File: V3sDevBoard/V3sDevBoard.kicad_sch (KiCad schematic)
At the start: 0 parts

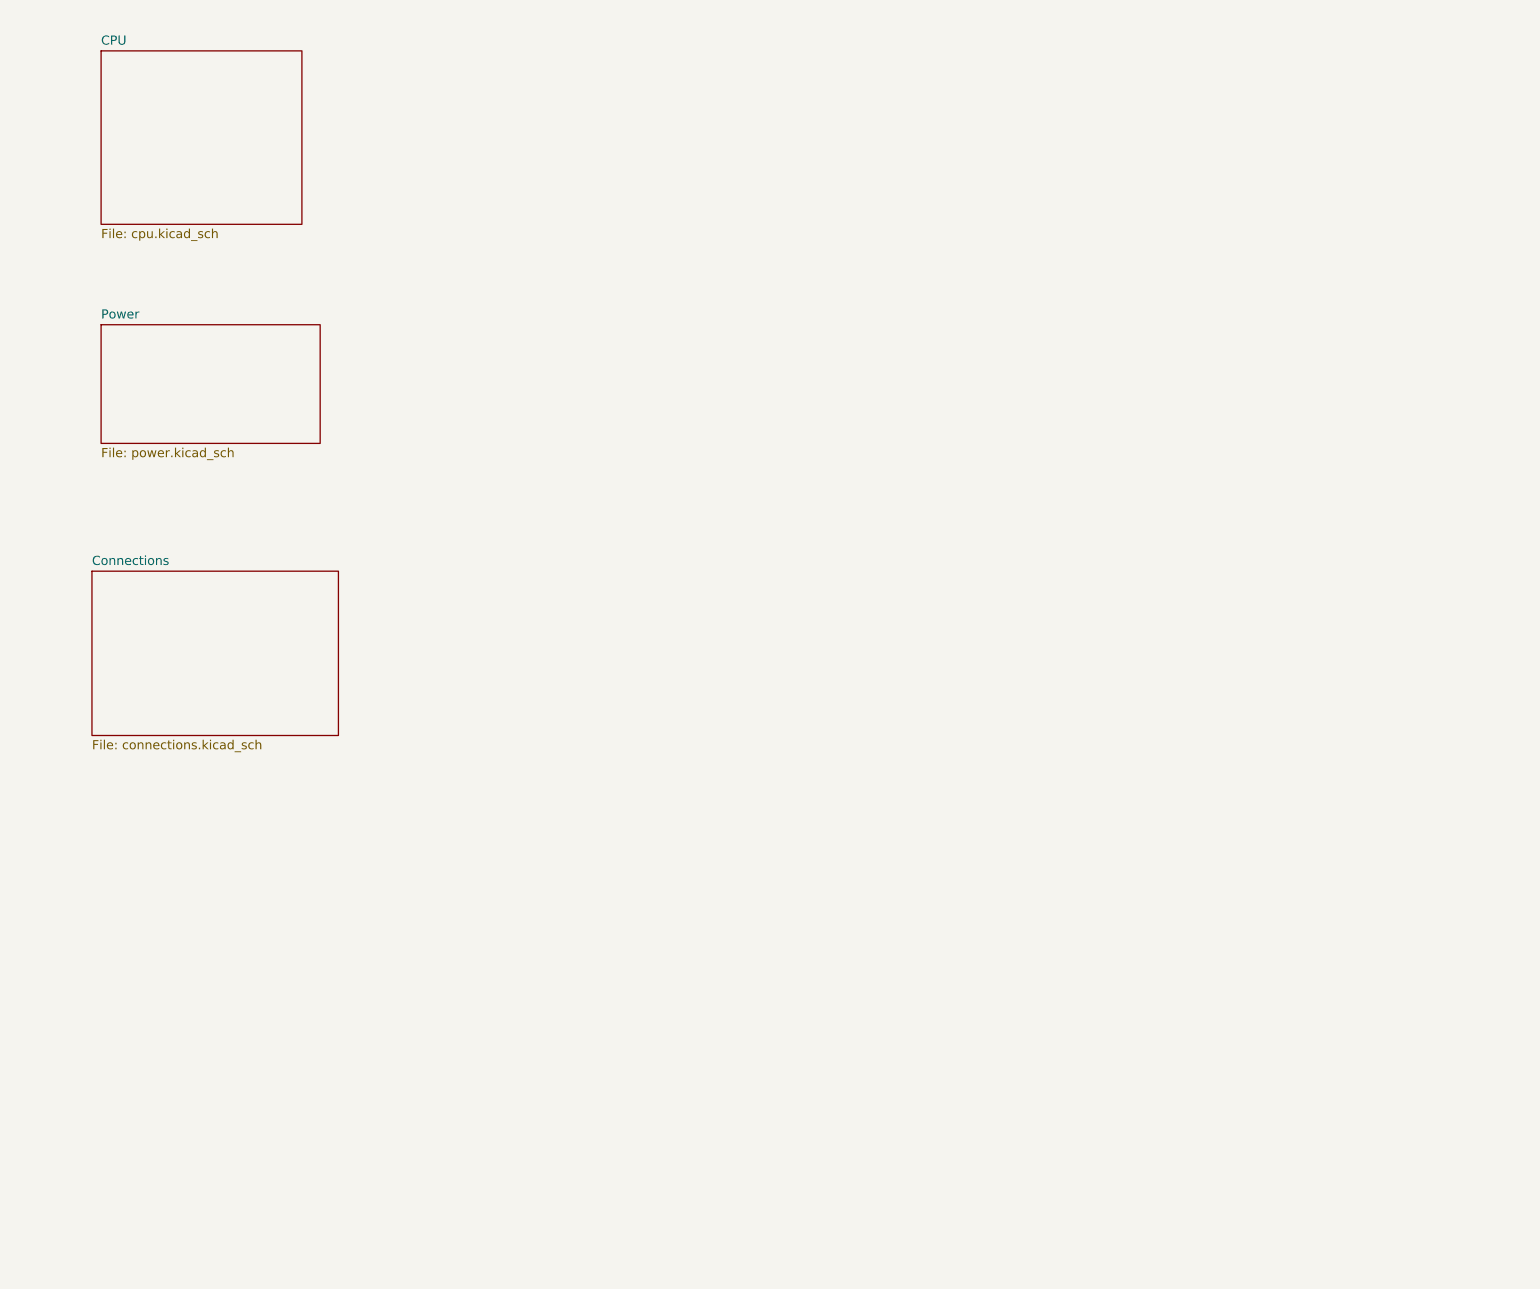
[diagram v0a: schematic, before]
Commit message: drawing schematic
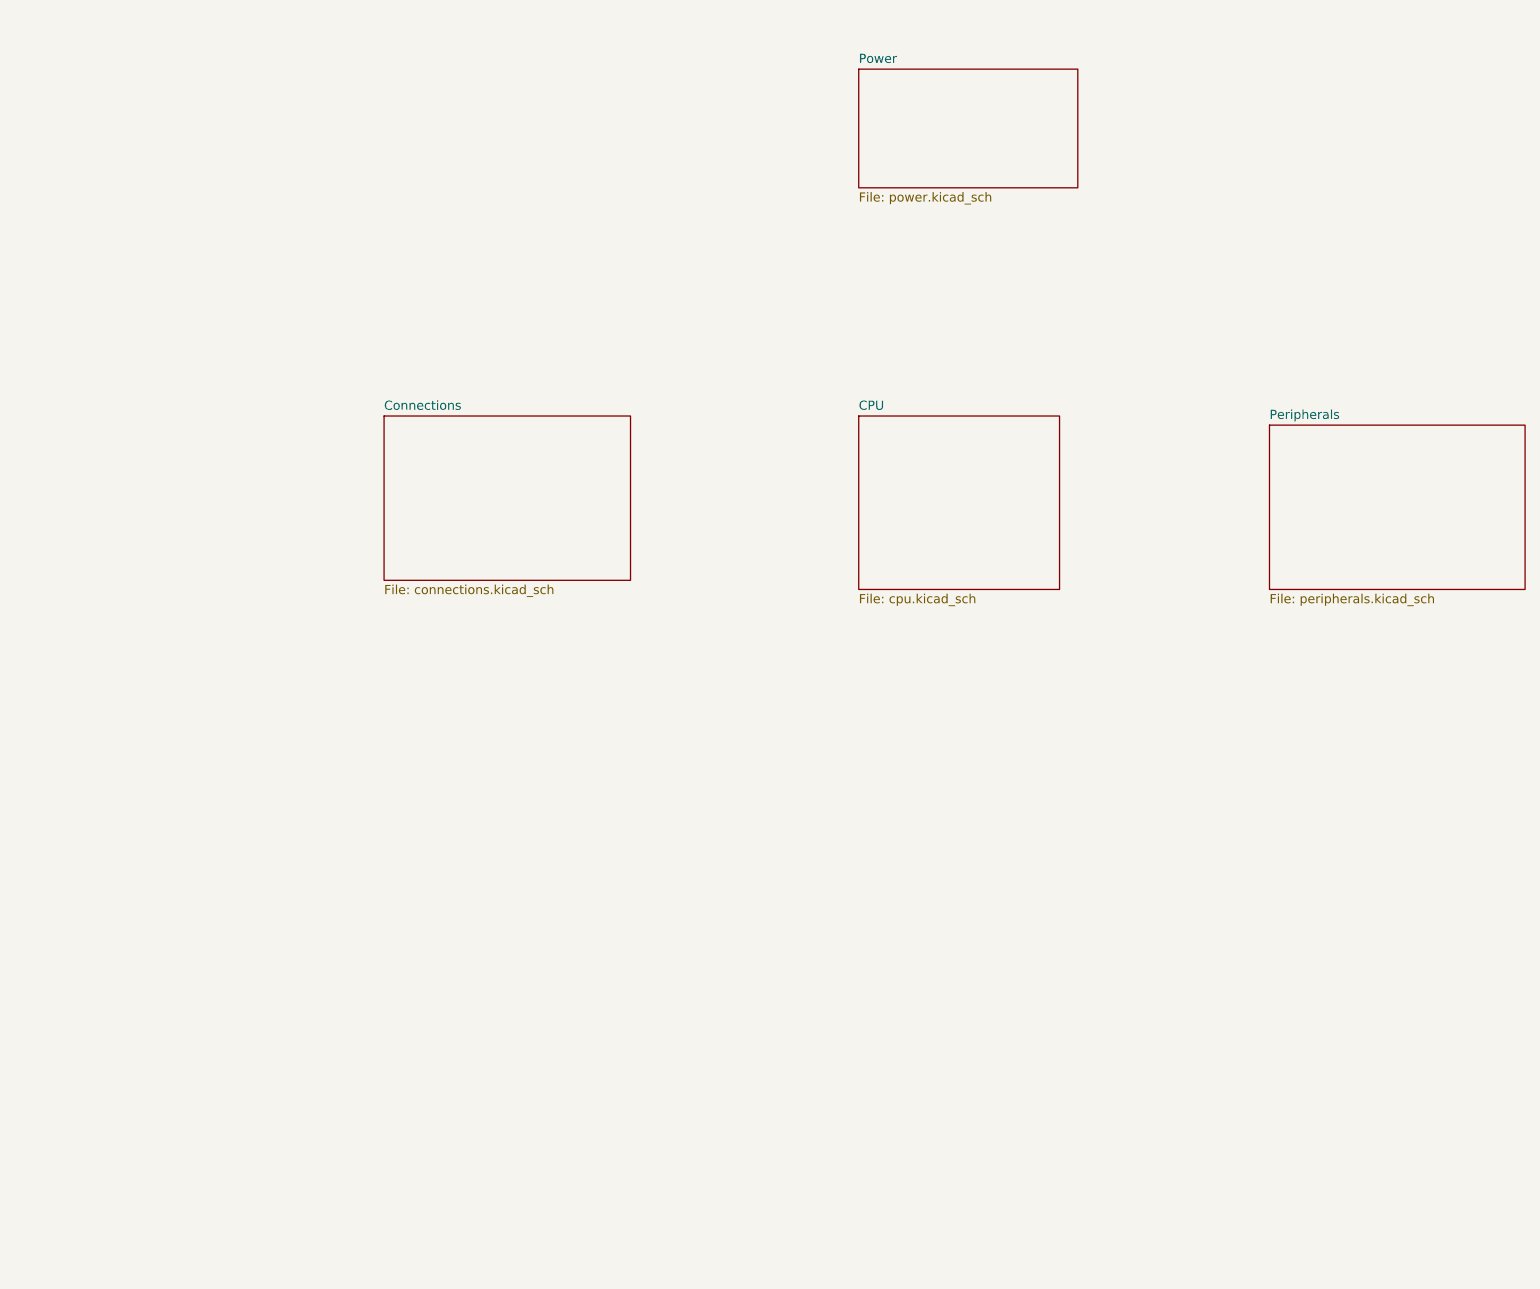
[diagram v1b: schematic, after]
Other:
- added sheet Peripherals (peripherals.kicad_sch)
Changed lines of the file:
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@@
 	(paper "A4")
 	(sheet
-		(at 25.4 99.06)
+		(at 66.04 77.47)
 		(size 34.29 22.86)
 		(exclude_from_sim no)
@@
 		)
 		(property "Sheetname" "Connections"
-			(at 25.4 98.3484 0)
+			(at 66.04 76.7584 0)
 			(effects
 				(font
@@
 		)
 		(property "Sheetfile" "connections.kicad_sch"
-			(at 25.4 122.5046 0)
+			(at 66.04 100.9146 0)
 			(effects
 				(font
@@
 	)
 	(sheet
-		(at 26.67 26.67)
+		(at 132.08 77.47)
 		(size 27.94 24.13)
 		(exclude_from_sim no)
@@
 		)
 		(property "Sheetname" "CPU"
-			(at 26.67 25.9584 0)
+			(at 132.08 76.7584 0)
 			(effects
 				(font
@@
 		)
 		(property "Sheetfile" "cpu.kicad_sch"
-			(at 26.67 51.3846 0)
+			(at 132.08 102.1846 0)
 			(effects
 				(font
@@
 	)
 	(sheet
-		(at 26.67 64.77)
+		(at 189.23 78.74)
+		(size 35.56 22.86)
+		(exclude_from_sim no)
+		(in_bom yes)
+		(on_board yes)
+		(dnp no)
+		(fields_autoplaced yes)
+		(stroke
+			(width 0.1524)
+			(type solid)
+		)
+		(fill
+			(color 0 0 0 0.0000)
+		)
+		(property "Sheetname" "Peripherals"
+			(at 189.23 78.0284 0)
+			(effects
+				(font
+					(size 1.27 1.27)
+				)
+				(justify left bottom)
+			)
+		)
+		(property "Sheetfile" "peripherals.kicad_sch"
+			(at 189.23 102.1846 0)
+			(effects
+				(font
+					(size 1.27 1.27)
+				)
+				(justify left top)
+			)
+		)
+		(instances
+			(project "V3sDevBoard"
+				(path "/e07febb4-5889-4da3-b279-3be53a5a6756"
+					(page "5")
+				)
+			)
+		)
+	)
+	(sheet
+		(at 132.08 29.21)
 		(size 30.48 16.51)
 		(exclude_from_sim no)
@@
 		)
 		(property "Sheetname" "Power"
-			(at 26.67 64.0584 0)
+			(at 132.08 28.4984 0)
 			(effects
 				(font
@@
 		)
 		(property "Sheetfile" "power.kicad_sch"
-			(at 26.67 81.8646 0)
+			(at 132.08 46.3046 0)
 			(effects
 				(font

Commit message: drawing schematics
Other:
- company: (none) -> J.K.
- title: (none) -> V3s Dev Board
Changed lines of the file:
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@@
 	(generator_version "9.0")
 	(paper "A4")
+	(title_block
+		(title "V3s Dev Board")
+		(date "2025/2026")
+		(rev "0.9")
+		(company "J.K.")
+	)
 	(sheet
 		(at 66.04 77.47)

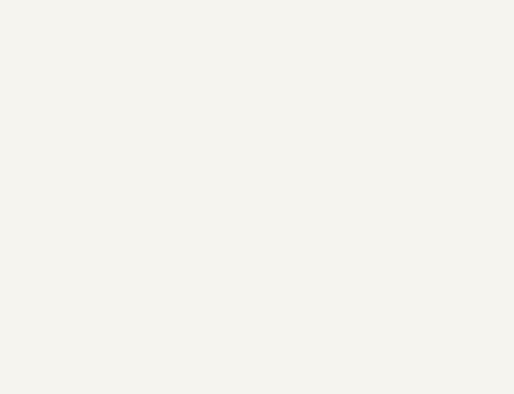
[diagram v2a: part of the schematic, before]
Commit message: advancing in schematics and footprints
Making needed custom footprints for connectors, adding a lot of small changes to schematics.
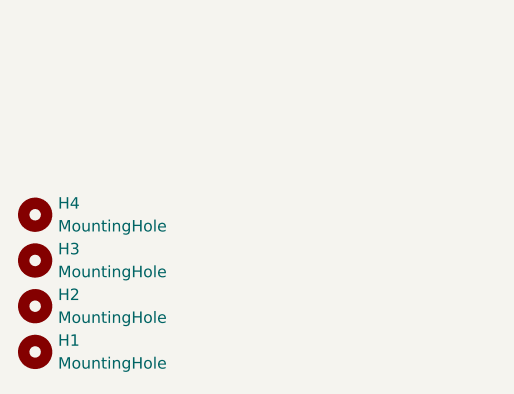
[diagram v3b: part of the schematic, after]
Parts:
- added H1, H2, H3, H4: MountingHole, MountingHole:MountingHole_3.2mm_M3, symbol Mechanical:MountingHole
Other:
- title: V3s Dev Board -> V3s_Dev_Board

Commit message: completing schematics
completing schematics, adding netclasses, fixing bugs, updating readme, starting pcb
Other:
- company: J.K. -> jakub.kmiecik@protonmail.com
- moved on the sheet: H1, H2, H3, H4
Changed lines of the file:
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@@
 		(date "2025/2026")
 		(rev "A")
-		(company "J.K.")
-		(comment 1 "SBC prototype for educational purposes, my first project of its kind.")
+		(company "jakub.kmiecik@protonmail.com")
+	)
+	(text_box "SYSTEM SPECIFICATIONS\n=====================\n\nCORE SYSTEM:\n- CPU: Allwinner V3s (ARM Cortex-A7 @ 1.2GHz)\n- RAM: 64MB DDR2 @ 400MHz (Integrated SiP)\n- STORAGE: SD Interface for OS (SDIO compatible)\n\nCONNECTIVITY:\n- ETHERNET: 100Mbps Interface\n- WIRELESS: WiFi & Bluetooth (via ESP32)\n- LONG RANGE: LoRa support (via Ra-02)\n- USB: USB Host/OTG support\n- DEBUG: System UARTs to USB bridge\n\nDISPLAY & IMAGING:\n- CAMERA: MIPI CSI (22-pin connector)\n- LCD: RGB-666 Interface with backlight support (40-pin)\n\nSENSORS & I/O:\n- MOTION: MPU6050 Accelerometer & Gyroscope\n- ENVIRONMENT: BME280 Sensor (Temp/Press/Hum)\n- AUDIO: 3.5mm Audio Jack\n- INPUT: Low-resolution ADC for button matrix\n- VISUAL: PCB RGB backlight\n\nPOWER & SOFTWARE:\n- REGULATION: DC-DC converters for 3.3V, 1.8V, 1.2V\n- OPERATING SYSTEM: Powered by custom Mainline Linux"
+		(exclude_from_sim no)
+		(at 19.05 21.59 0)
+		(size 93.98 116.84)
+		(margins 0.9525 0.9525 0.9525 0.9525)
+		(stroke
+			(width 0)
+			(type solid)
+		)
+		(fill
+			(type none)
+		)
+		(effects
+			(font
+				(size 1.5 1.5)
+			)
+			(justify left top)
+		)
 	)
 	(symbol
 		(lib_id "Mechanical:MountingHole")
-		(at 48.26 177.8 0)
+		(at 16.51 189.23 0)
 		(unit 1)
 		(exclude_from_sim no)
@@
 		(fields_autoplaced yes)
 		(property "Reference" "H2"
-			(at 50.8 176.5299 0)
+			(at 19.05 187.9599 0)
 			(effects
 				(font
@@
 		)
 		(property "Value" "MountingHole"
-			(at 50.8 179.0699 0)
+			(at 19.05 190.4999 0)
 			(effects
 				(font
@@
 		)
 		(property "Footprint" "MountingHole:MountingHole_3.2mm_M3"
-			(at 48.26 177.8 0)
+			(at 16.51 189.23 0)
 			(effects
 				(font
@@
 		)
 		(property "Datasheet" "~"
-			(at 48.26 177.8 0)
+			(at 16.51 189.23 0)
 			(effects
 				(font
@@
 		)
 		(property "Description" "Mounting Hole without connection"
-			(at 48.26 177.8 0)
+			(at 16.51 189.23 0)
 			(effects
 				(font
@@
 	(symbol
 		(lib_id "Mechanical:MountingHole")
-		(at 48.26 182.88 0)
+		(at 16.51 194.31 0)
 		(unit 1)
 		(exclude_from_sim no)
@@
 		(fields_autoplaced yes)
 		(property "Reference" "H1"
-			(at 50.8 181.6099 0)
+			(at 19.05 193.0399 0)
 			(effects
 				(font
@@
 		)
 		(property "Value" "MountingHole"
-			(at 50.8 184.1499 0)
+			(at 19.05 195.5799 0)
 			(effects
 				(font
@@
 		)
 		(property "Footprint" "MountingHole:MountingHole_3.2mm_M3"
-			(at 48.26 182.88 0)
+			(at 16.51 194.31 0)
 			(effects
 				(font
@@
 		)
 		(property "Datasheet" "~"
-			(at 48.26 182.88 0)
+			(at 16.51 194.31 0)
 			(effects
 				(font
@@
 		)
 		(property "Description" "Mounting Hole without connection"
-			(at 48.26 182.88 0)
+			(at 16.51 194.31 0)
 			(effects
 				(font
@@
 	(symbol
 		(lib_id "Mechanical:MountingHole")
-		(at 48.26 167.64 0)
+		(at 16.51 179.07 0)
 		(unit 1)
 		(exclude_from_sim no)
@@
 		(fields_autoplaced yes)
 		(property "Reference" "H4"
-			(at 50.8 166.3699 0)
+			(at 19.05 177.7999 0)
 			(effects
 				(font
@@
 		)
 		(property "Value" "MountingHole"
-			(at 50.8 168.9099 0)
+			(at 19.05 180.3399 0)
 			(effects
 				(font
@@
 		)
 		(property "Footprint" "MountingHole:MountingHole_3.2mm_M3"
-			(at 48.26 167.64 0)
+			(at 16.51 179.07 0)
 			(effects
 				(font
@@
 		)
 		(property "Datasheet" "~"
-			(at 48.26 167.64 0)
+			(at 16.51 179.07 0)
 			(effects
 				(font
@@
 		)
 		(property "Description" "Mounting Hole without connection"
-			(at 48.26 167.64 0)
+			(at 16.51 179.07 0)
 			(effects
 				(font
@@
 	(symbol
 		(lib_id "Mechanical:MountingHole")
-		(at 48.26 172.72 0)
+		(at 16.51 184.15 0)
 		(unit 1)
 		(exclude_from_sim no)
@@
 		(fields_autoplaced yes)
 		(property "Reference" "H3"
-			(at 50.8 171.4499 0)
+			(at 19.05 182.8799 0)
 			(effects
 				(font
@@
 		)
 		(property "Value" "MountingHole"
-			(at 50.8 173.9899 0)
+			(at 19.05 185.4199 0)
 			(effects
 				(font
@@
 		)
 		(property "Footprint" "MountingHole:MountingHole_3.2mm_M3"
-			(at 48.26 172.72 0)
+			(at 16.51 184.15 0)
 			(effects
 				(font
@@
 		)
 		(property "Datasheet" "~"
-			(at 48.26 172.72 0)
+			(at 16.51 184.15 0)
 			(effects
 				(font
@@
 		)
 		(property "Description" "Mounting Hole without connection"
-			(at 48.26 172.72 0)
+			(at 16.51 184.15 0)
 			(effects
 				(font
@@
 	)
 	(sheet
-		(at 66.04 77.47)
+		(at 189.23 29.21)
 		(size 34.29 22.86)
 		(exclude_from_sim no)
@@
 		)
 		(property "Sheetname" "Connections"
-			(at 66.04 76.7584 0)
-			(effects
-				(font
-					(size 1.27 1.27)
+			(at 189.23 27.6334 0)
+			(effects
+				(font
+					(size 3 3)
 				)
 				(justify left bottom)
@@
 		)
 		(property "Sheetfile" "connections.kicad_sch"
-			(at 66.04 100.9146 0)
+			(at 189.23 52.6546 0)
 			(effects
 				(font
@@
 		)
 		(property "Sheetname" "CPU"
-			(at 132.08 76.7584 0)
-			(effects
-				(font
-					(size 1.27 1.27)
+			(at 132.08 75.8934 0)
+			(effects
+				(font
+					(size 3 3)
 				)
 				(justify left bottom)
@@
 		)
 		(property "Sheetname" "Peripherals"
-			(at 189.23 78.0284 0)
-			(effects
-				(font
-					(size 1.27 1.27)
+			(at 189.23 77.1634 0)
+			(effects
+				(font
+					(size 3 3)
 				)
 				(justify left bottom)
@@
 			(effects
 				(font
-					(size 1.27 1.27)
+					(size 3 3)
 				)
 				(justify left bottom)
